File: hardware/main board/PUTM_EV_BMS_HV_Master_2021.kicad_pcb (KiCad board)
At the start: 4 copper layers, 60 x 150 mm, 246 parts, among them IC1 MCP1501-10E_SN, IC10 REF193GSZ-REEL, IC11 AP7365-33YRG-13, IC12 UCC12040DVE, IC13 MAX17643ATC+, IC14 RTQ2965GSP-QA, IC15 ISO6763FDWR, IC16 ISO6763FDWR, IC17 UCC12040DVE, IC2 MCP3561T-E_NC, IC3 REF193GSZ-REEL, IC4 MCP3561T-E_NC, IC6 AP7365-33YRG-13, IC7 MCP3562T-E_NC, IC9 REF193GSZ-REEL, J1 USB4145-03-0070-C, J10 M80-5100622, J11 M80-5101422, J14 Conn_01x05, J16 TagConnect, J2 M80-5100442, J3 M80-5100442, J4 M300-MV10345M1, J5 M300-MV10345M1, J6 M80-5100442, J7 M80-5100622, J8 M80-5102022, J9 M300-MV30645M1, K2 6-1419128-4, Q1 2SK3065, Q10 Q_NMOS_GSD, Q11 Q_NMOS_GSD, Q12 2SK3065, Q13 2SK3065, Q14 2SK3065, Q15 2SK3065, Q2 2N7002, Q3 Q_NMOS_GDS, Q4 2N7002, Q5 Q_NMOS_GDS, Q6 Q_NMOS_GDS, Q7 2SK3065, Q8 Q_PMOS_GSD, Q9 2SK3065, T1 HX1188NL, U12 LTC6820IMS, U13 LTC6820IMS, U14 74AUP1G32, U2 STM32G484RETx, U3 MCP2542FDxMF, U4 USBLC6-2SC6, U5 LM1117-3.3, U6 MCP2542FDxMF, U8 74LVC1G86, Y1 20MHz, Y2 32.768kHz

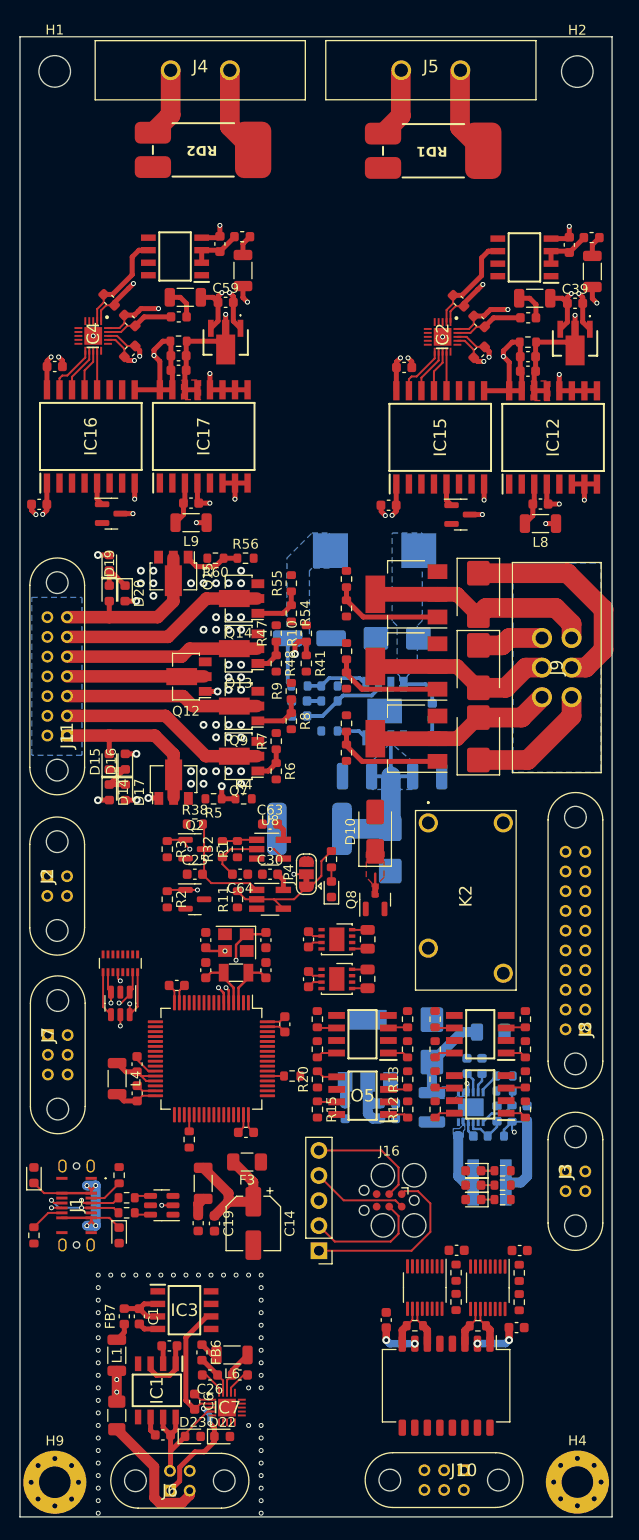
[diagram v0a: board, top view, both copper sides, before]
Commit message: step + rounded pcb corners
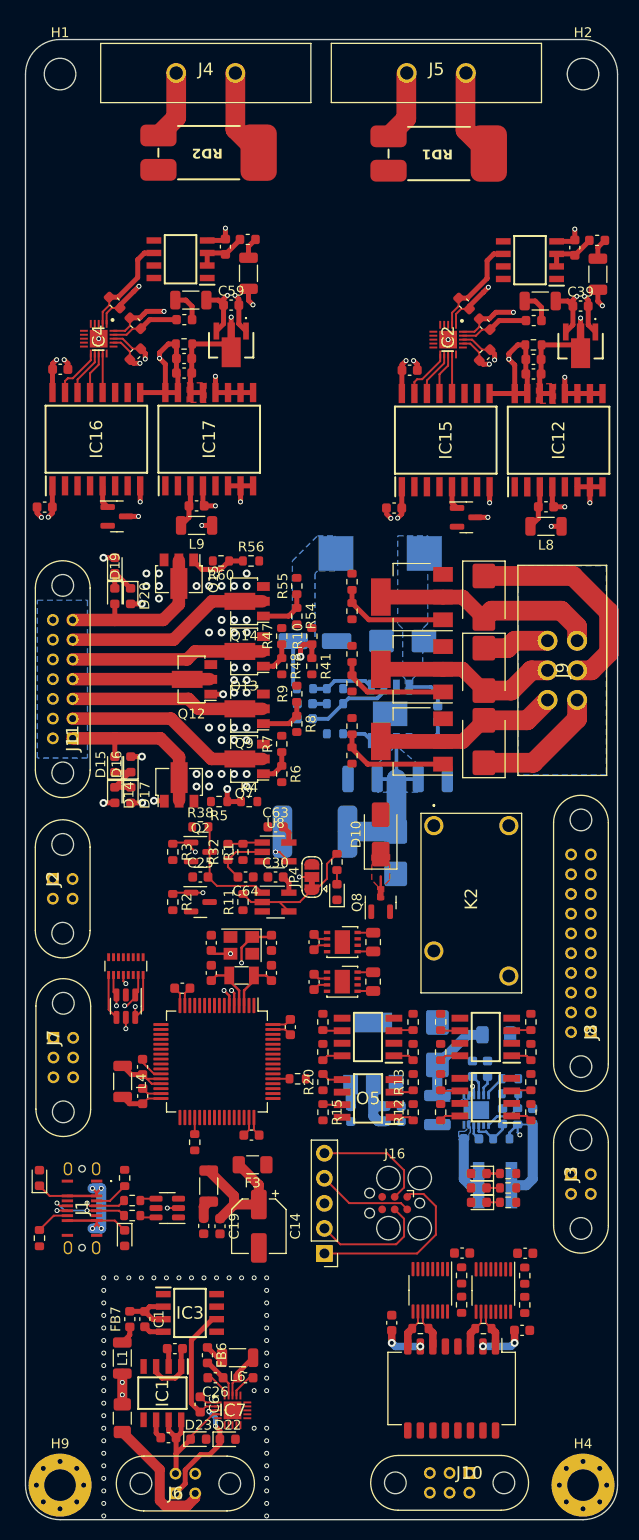
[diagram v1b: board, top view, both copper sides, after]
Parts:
- moved H4 0.65 mm to (163.5, 179.5)
- moved H2 0.63 mm to (163.5, 36.5)
- moved C1 0.63 mm to (119.1, 162.7)
- moved C12 0.63 mm to (140.0, 141.9)
- moved C13 0.63 mm to (153.5, 65.0)
- moved C17 0.63 mm to (145.9, 66.5)
- moved C2 0.63 mm to (122.1, 165.7)
- moved C20 0.63 mm to (151.4, 59.8)
- moved C21 0.63 mm to (142.2, 128.5)
- moved C23 0.63 mm to (118.1, 64.9)
- moved C24 0.63 mm to (148.7, 141.5)
- moved C29 0.63 mm to (144.1, 163.1)
- moved C30 0.63 mm to (132.3, 117.9)
- moved C31 0.63 mm to (110.5, 66.4)
- moved C35 0.63 mm to (151.2, 156.0)
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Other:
- outline, holes or cut-outs redrawn

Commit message: sync
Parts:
- moved C12 0.75 mm to (139.2, 141.9)
- moved C15 0.75 mm to (143.5, 141.1)
- moved C16 0.75 mm to (143.5, 142.6)
- moved U5 0.75 mm to (141.5, 135.8)
- moved C68 0.57 mm to (159.0, 142.1)
- moved F2 0.57 mm to (155.3, 133.9)
- moved R51 0.57 mm to (157.4, 142.1)
- moved C24 0.57 mm to (149.3, 141.5)
- moved C65 0.57 mm to (152.7, 144.4)
- moved C66 0.57 mm to (155.9, 142.1)
- moved C67 0.57 mm to (154.4, 137.3)
- moved C69 0.57 mm to (152.9, 137.3)
- moved D11 0.57 mm to (149.3, 134.8)
- moved IC13 0.57 mm to (153.2, 141.5)
- moved L11 0.57 mm to (155.2, 149.1)
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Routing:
- net GND: track 51.4 -> 55.5 mm
- added copper zone on B.Cu, net GND
- added copper zone on F.Cu, net GND
- added copper zone on In1.Cu, net GND
- added copper zone on In2.Cu, net GND

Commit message: done power plane layout
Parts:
- removed J3: M80-5100442, Samacsys:M80-51004YY
- removed J7: M80-5100622, Samacsys:M80-51006YY
- removed J8: M80-5102022, Samacsys:M80-51020YY
- added C8: 47uF, Capacitor_SMD:C_0603_1608Metric, B.Cu at (143.4, 136.1)
- added R21: 10k, Resistor_SMD:R_0603_1608Metric, F.Cu at (114.5, 143.5)
- C68: value 22uF -> 47uF
- J2: value M80-5100442 -> M80-5103422; footprint Samacsys:M80-51004YY -> Samacsys:M80-51034YY
- moved J2 52.5 mm to (162.2, 116.0)
- moved R19 42.4 mm to (110.0, 112.1), turned to 180 degrees
- moved D7 42.2 mm to (118.5, 123.6)
- moved R69 42.2 mm to (121.4, 126.5)
- moved D5 42.2 mm to (118.5, 126.5)
- moved D6 42.2 mm to (118.5, 125.0)
- moved R71 42.2 mm to (121.4, 125.0)
- moved R72 42.2 mm to (121.4, 123.6)
- moved D21 37.1 mm to (116.1, 112.1), turned to 0 degrees
- moved J1 35.0 mm to (113.0, 116.4), turned to 180 degrees
- moved D1 34.5 mm to (110.0, 120.7), turned to 180 degrees
- moved D8 33.9 mm to (147.5, 146.1), turned to 0 degrees
- moved RN2 32.5 mm to (143.4, 146.1), turned to 0 degrees
- moved R50 31.2 mm to (112.3, 121.5), turned to -90 degrees
- moved R49 29.4 mm to (113.8, 121.5), turned to 90 degrees
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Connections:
- J2 pad 1: GND -> SAFETY_TSMS_IN
- J2 pad 2: AIR_PRE_DETECTION -> VDD
- J2 pad 3: AIR_P_DETECTION -> GND
- J2 pad 4: AIR_M_DETECTION -> AMS_SAFETY_1
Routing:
- net +3V3: track 64.8 -> 113.8 mm, vias 4 -> 28
- net Net-(D3-K): track 18.4 -> 0.00 mm
- net +12V: track 14.5 -> 29.8 mm
- net AMS_SAFETY_1: track 0.00 -> 15.3 mm
- net +5V: track 20.9 -> 8.55 mm, vias 6 -> 5
- net Net-(D10-K): track 1.70 -> 9.77 mm
- net AMS_SAFETY_2: track 0.00 -> 7.89 mm
- net /Safeties and related/AMS_FAULT: track 14.1 -> 21.1 mm
- net Net-(IC13-LX): track 5.85 -> 0.00 mm
- net Net-(U12-ICMP): track 0.00 -> 4.28 mm
- net Net-(U13-ICMP): track 0.00 -> 4.27 mm
- net SWCLK: track 12.2 -> 8.45 mm, vias 0 -> 1
- net VBUS: track 21.5 -> 18.4 mm, vias 4 -> 7
- net GND: track 55.5 -> 58.3 mm, vias 100 -> 96
- net NRST: track 14.0 -> 16.0 mm, vias 0 -> 1
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- added copper zone on B.Cu, net +3V3
- added copper zone on B.Cu, net +5V
- added copper zone on F.Cu, net +5V
- added copper zone on B.Cu, net Net-(D6-K)
- added copper zone on B.Cu, net VBUS
- added copper zone on F.Cu, net VBUS
- added copper zone on B.Cu, net VDD
- removed copper zone on In1.Cu, net +12V
- removed copper zone on B.Cu, net Net-(D2-K)
- removed copper zone on In1.Cu, net SAFETY_TSMS_IN
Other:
- board text added: "LV"
- board text added: "TS"

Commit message: repairing demaged branch~
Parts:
- added FL1: DLW21SN501SK2L, Samacsys:DLW21SN121HQ2L, F.Cu at (156.2, 145.1)
- added R25: 10M, Resistor_SMD:R_2512_6332Metric, F.Cu at (161.8, 162.0)
- added R26: 33, Resistor_SMD:R_0603_1608Metric, F.Cu at (140.0, 146.1)
- added R36: 33, Resistor_SMD:R_0603_1608Metric, F.Cu at (140.0, 144.1)
- added U1: USBLC6-2SC6, Package_TO_SOT_SMD:SOT-23-6, F.Cu at (136.4, 145.1)
- H4: footprint MountingHole:MountingHole_3.2mm_M3_Pad_Via -> MountingHole:MountingHole_3.2mm_M3
- moved C3 21.2 mm to (149.6, 86.8), turned to 90 degrees
- moved C72 19.4 mm to (117.0, 92.6), turned to 90 degrees
- moved C11 18.0 mm to (149.6, 92.0), turned to -90 degrees
- moved C71 17.2 mm to (143.0, 85.1), turned to 180 degrees
- moved L3 17.0 mm to (126.8, 90.2), turned to -90 degrees
- moved D3 16.9 mm to (150.2, 97.0)
- moved L11 14.7 mm to (141.2, 117.4)
- moved R59 14.7 mm to (142.7, 106.6)
- moved C24 14.7 mm to (135.3, 109.8)
- moved C65 14.7 mm to (138.8, 112.7)
- moved C66 14.7 mm to (141.9, 110.4)
- moved C67 14.7 mm to (140.4, 105.6)
- moved C68 14.7 mm to (145.0, 110.4)
- moved C69 14.7 mm to (138.9, 105.6)
- moved C8 14.7 mm to (143.6, 121.4)
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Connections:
- J2 pad 10: VBUS -> CHARGER_DETECTION
- J2 pad 11: AIR_M_DETECTION -> EXT_RESET
- J2 pad 13: IMD_SENSENSOR -> AIR_M_DETECTION
- J2 pad 16: GND -> EX_D-
- J2 pad 17: GND -> EX_D+
- J2 pad 22: EXT_RESET -> GND
- J2 pad 24: CANFD2- -> CANFD1-
- J2 pad 25: CANFD2+ -> CANFD2-
- J2 pad 26: CANFD1- -> GND
- J2 pad 27: CANFD1+ -> GND
- J2 pad 29: GND -> BOOT0
- J2 pad 30: GND -> IMD_SENSENSOR
- J2 pad 34: GND -> EX_VBUS
- J2 pad 6: CHARGER_DETECTION -> GND
- J2 pad 7: D+ -> CANFD1+
- J2 pad 8: D- -> CANFD2+
- J2 pad 9: BOOT0 -> GND
- JP4 pad 3: /Safeties and related/AMS_FAULT_LED -> /MCU_LED_3
- R10 pad 2: /Fan drivers/FAN4_CTRL -> /FAN_4_CTRL
- R4 pad 2: /Fan drivers/FAN1_CTRL -> /FAN_1_CTRL
- R40 pad 2: SAFETY_TSMS_IN -> CHARGER_DETECTION
- R44 pad 2: CHARGER_DETECTION -> SAFETY_TSMS_IN
- R47 pad 2: /Fan drivers/FAN5_CTRL -> /FAN_5_CTRL
- R54 pad 2: /Fan drivers/FAN6_CTRL -> /FAN_6_CTRL
- R56 pad 2: /Fan drivers/FAN7_CTRL -> /FAN_7_CTRL
- R6 pad 2: /Fan drivers/FAN2_CTRL -> /FAN_2_CTRL
- R8 pad 2: /Fan drivers/FAN3_CTRL -> /FAN_3_CTRL
- U2 pad 39: /SIGNAL_AIR_M -> /SIGNAL_AIR_PRE
- U2 pad 41: /SIGNAL_AIR_PRE -> /SIGNAL_AIR_M
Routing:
- net SCK: track 0.00 -> 184.7 mm, vias 0 -> 5
- net MOSI: track 0.00 -> 184.5 mm, vias 0 -> 5
- net MISO: track 1.68 -> 179.4 mm, vias 0 -> 5
- net /~{MES_CAR_CS}: track 0.00 -> 123.3 mm, vias 0 -> 2
- net /~{MES_ACU_CS}: track 0.00 -> 95.5 mm, vias 0 -> 2
- net /SIGNAL_AIR_M: track 0.00 -> 68.3 mm, vias 0 -> 2
- net /SIGNAL_AIR_P: track 0.00 -> 60.6 mm, vias 0 -> 2
- net /FAN_7_CTRL: track 0.00 -> 59.4 mm, vias 0 -> 2
- net /FAN_5_CTRL: track 0.00 -> 53.8 mm, vias 0 -> 2
- net /SIGNAL_AIR_PRE: track 0.00 -> 52.8 mm, vias 0 -> 2
- net /FAN_6_CTRL: track 0.00 -> 49.8 mm, vias 0 -> 2
- net /FAN_4_CTRL: track 0.00 -> 47.0 mm, vias 0 -> 2
- net NRST: track 16.0 -> 62.8 mm, vias 1 -> 3
- net /LTC_SCK: track 0.00 -> 42.1 mm, vias 0 -> 3
- net /AMS_FAULT_MCU: track 3.53 -> 45.4 mm, vias 0 -> 2
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- added copper zone on F.Cu, net /Connectors/LTC_CHASSIS
- added copper zone on In1.Cu, net /Connectors/LTC_CHASSIS
- added copper zone on In2.Cu, net /Connectors/LTC_CHASSIS
- added copper zone on F.Cu, net /Measurements/Isolated acu measurement/HV_MES+
- added copper zone on F.Cu, net /Measurements/Isolated car measurement/HV_MES+
- added copper zone on B.Cu, net Net-(D2-K)
- added copper zone on F.Cu, net VDD
- removed copper zone on B.Cu, net Net-(D6-K)
